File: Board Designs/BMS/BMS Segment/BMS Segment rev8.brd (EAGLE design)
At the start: 108 x 247.1 mm, 267 parts

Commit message: Moved 6804 inward, fixed clearance issues
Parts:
- moved RU1_A 37.3 mm to (65.0, 228.6)
- moved J1_A 9.02 mm to (105.7, 198.5)
- moved J2_A 9.02 mm to (103.8, 198.5)
- moved J3_A 9.02 mm to (101.9, 198.5)
- moved J4_A 9.02 mm to (100.0, 198.5)
- moved J5_A 9.02 mm to (98.1, 198.5)
- moved J6_A 9.02 mm to (96.2, 198.5)
- moved J7_A 9.02 mm to (94.3, 198.5)
- moved J8_A 9.02 mm to (92.4, 198.5)
- moved C1_A 7.62 mm to (104.8, 179.3)
- moved RB1_A 7.62 mm to (104.8, 188.8)
- moved RB2_A 7.62 mm to (104.8, 185.7)
- moved U$1 7.62 mm to (94.7, 185.1)
- moved C2_A 7.62 mm to (104.8, 182.5)
- moved C6_A 7.62 mm to (94.3, 194.1)
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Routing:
- net V-_A: track 804.3 -> 746.8 mm
- net UNUSED1_A: track 95.2 -> 64.8 mm
- net S5_B: track 136.6 -> 106.6 mm
- net V-_B: track 708.3 -> 685.2 mm
- net GPIO4_A: track 65.9 -> 76.6 mm
- net VREG_A: track 76.9 -> 66.9 mm
- net SENSE18: track 140.5 -> 132.8 mm
- net GPIO1_A: track 192.4 -> 200.1 mm
- net GPIO3_A: track 126.2 -> 133.9 mm
- net GPIO2_A: track 180.2 -> 187.9 mm
- net C9_A: track 67.8 -> 75.5 mm
- net C10_A: track 64.9 -> 72.5 mm
- net S9_A: track 71.1 -> 78.7 mm
- net C3_A: track 39.3 -> 31.8 mm
- net S3_A: track 32.9 -> 25.3 mm
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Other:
- board text added: "x1"
- board text added: "x2"
- board text added: "x4"
- board text added: "x8"

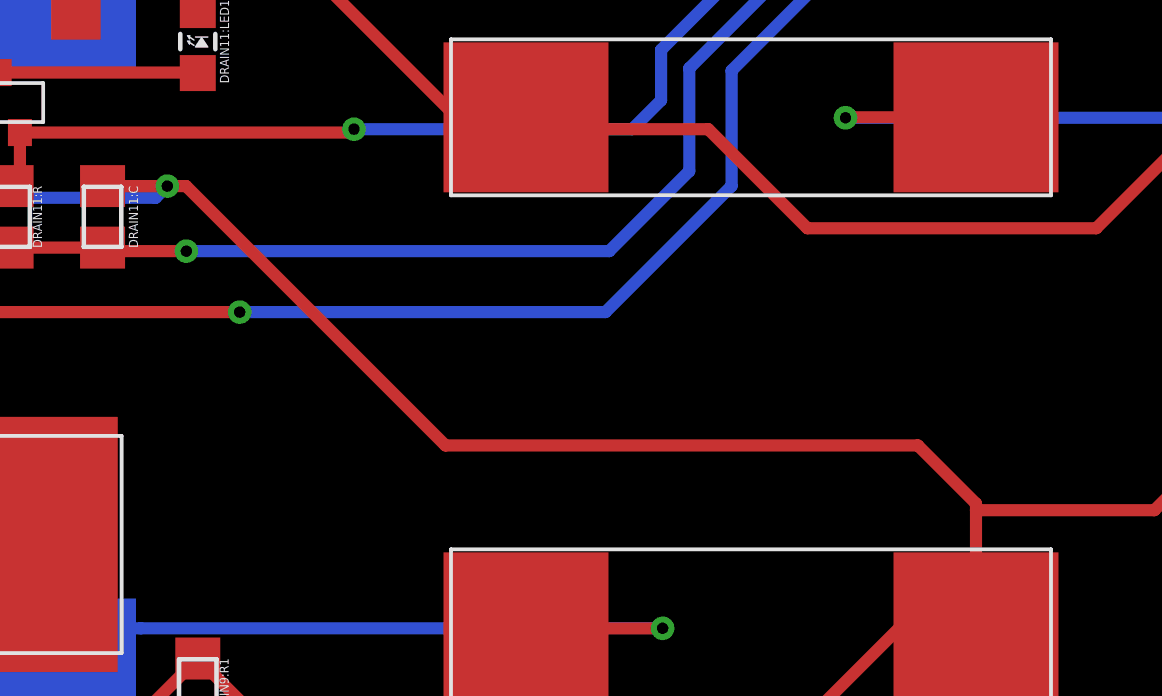
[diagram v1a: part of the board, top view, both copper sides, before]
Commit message: Changed resistor values to K, M, R convention. Changed texts to vector font
Eagle has the greek symbol ohm on the schematic and board in proportional font, but it does not have it in vector font. CAM processor seems to automatically convert to vector front and all the ohm symbol shows up as ? on the silkscreen.
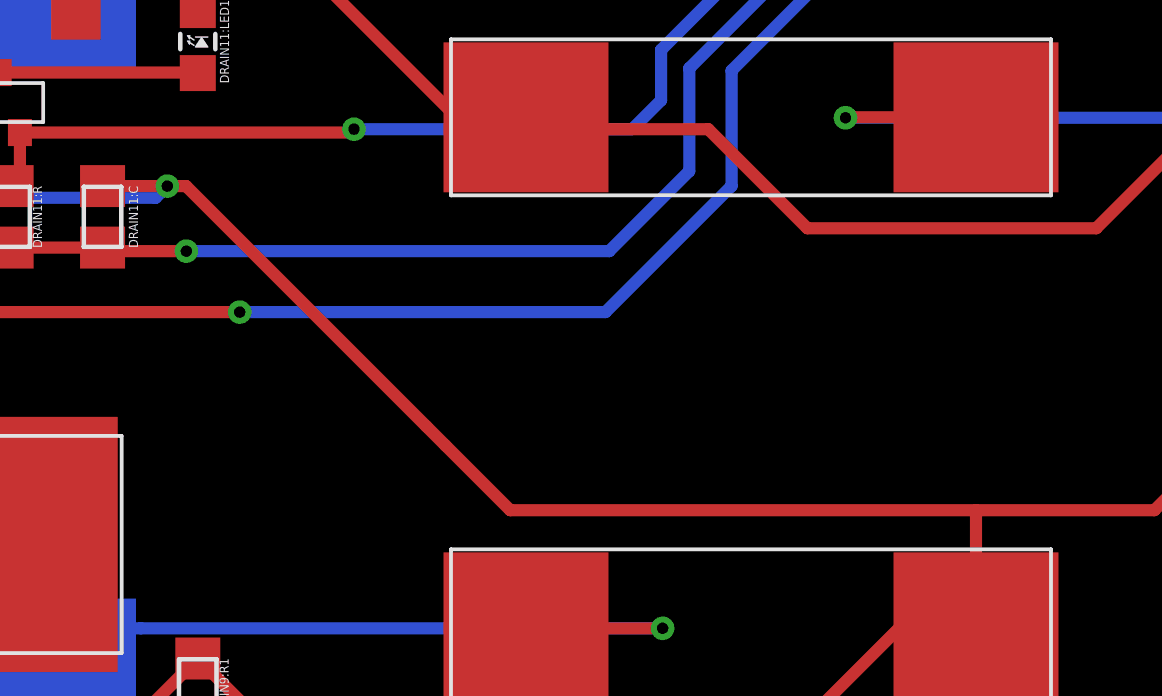
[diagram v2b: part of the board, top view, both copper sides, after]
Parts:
- DRAIN10:DISCHARGE, DRAIN11:DISCHARGE, DRAIN12:DISCHARGE, DRAIN13:DISCHARGE, DRAIN14:DISCHARGE, DRAIN15:DISCHARGE, DRAIN16:DISCHARGE, DRAIN17:DISCHARGE, DRAIN18:DISCHARGE, DRAIN1:DISCHARGE, DRAIN2:DISCHARGE, DRAIN3:DISCHARGE, DRAIN4:DISCHARGE, DRAIN5:DISCHARGE, DRAIN6:DISCHARGE, DRAIN7:DISCHARGE, DRAIN8:DISCHARGE, DRAIN9:DISCHARGE: value 5Ω -> 5R
- DRAIN10:GATE, DRAIN11:GATE, DRAIN12:GATE, DRAIN13:GATE, DRAIN14:GATE, DRAIN15:GATE, DRAIN16:GATE, DRAIN17:GATE, DRAIN18:GATE, DRAIN1:GATE, DRAIN2:GATE, DRAIN3:GATE, DRAIN4:GATE, DRAIN5:GATE, DRAIN6:GATE, DRAIN7:GATE, DRAIN8:GATE, DRAIN9:GATE: value 3.3kΩ -> 3K3
- DRAIN10:R, DRAIN11:R, DRAIN12:R, DRAIN13:R, DRAIN14:R, DRAIN15:R, DRAIN16:R, DRAIN17:R, DRAIN18:R, DRAIN1:R, DRAIN2:R, DRAIN3:R, DRAIN4:R, DRAIN5:R, DRAIN6:R, DRAIN7:R, DRAIN8:R, DRAIN9:R, R1_A, R1_B, R2_A, R2_B, RIN_A, RIN_B, RM_A, RM_B, RU1_A, RU1_B, THERM_FILTER10:R, THERM_FILTER1:R, THERM_FILTER2:R, THERM_FILTER3:R, THERM_FILTER4:R, THERM_FILTER5:R, THERM_FILTER6:R, THERM_FILTER7:R, THERM_FILTER8:R, THERM_FILTER9:R: value 100Ω -> 100R
- DRAIN10:R1, DRAIN11:R1, DRAIN12:R1, DRAIN13:R1, DRAIN14:R1, DRAIN15:R1, DRAIN16:R1, DRAIN17:R1, DRAIN18:R1, DRAIN1:R1, DRAIN2:R1, DRAIN3:R1, DRAIN4:R1, DRAIN5:R1, DRAIN6:R1, DRAIN7:R1, DRAIN8:R1, DRAIN9:R1: value 150Ω -> 150R
- R3_A, R3_B: value 402Ω -> 402R
- R4_A, R4_B, R5_A, R5_B: value 22Ω -> 22R
- RB1_A, RB1_B: value 1.2kΩ -> 1K2
- RB2_A, RB2_B: value 800Ω -> 800R
- THERM1, THERM2, THERM3, THERM4, THERM_FILTER10:R1, THERM_FILTER1:R1, THERM_FILTER2:R1, THERM_FILTER3:R1, THERM_FILTER4:R1, THERM_FILTER5:R1, THERM_FILTER6:R1, THERM_FILTER7:R1, THERM_FILTER8:R1, THERM_FILTER9:R1: value 10kΩ -> 10K

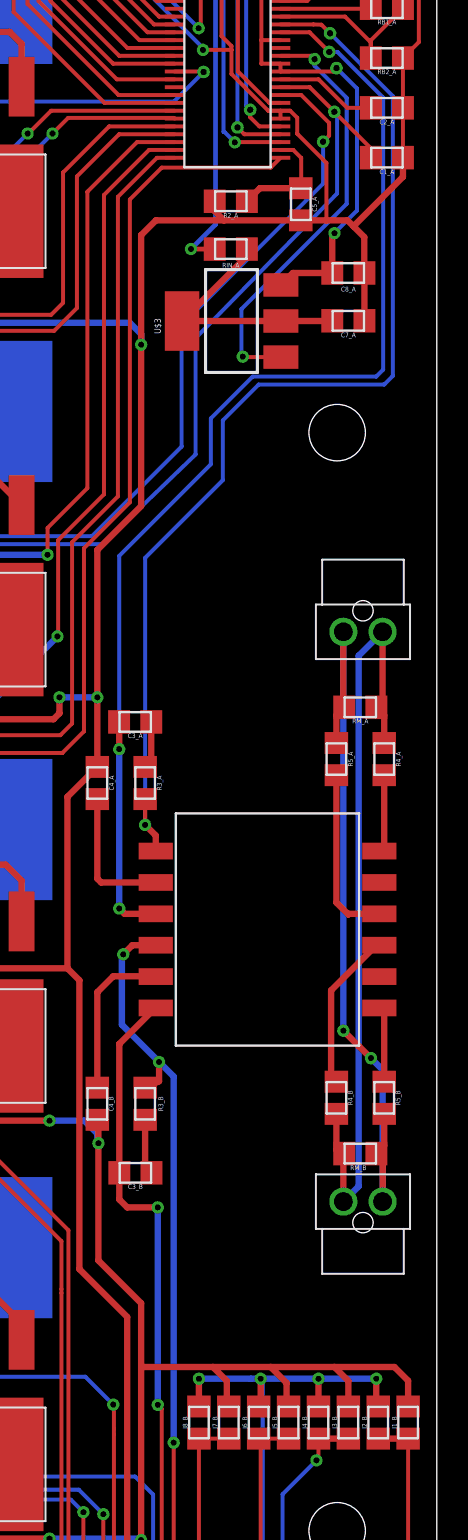
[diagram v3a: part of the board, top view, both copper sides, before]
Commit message: Silkscreen modifications, small adjustments to trace locations
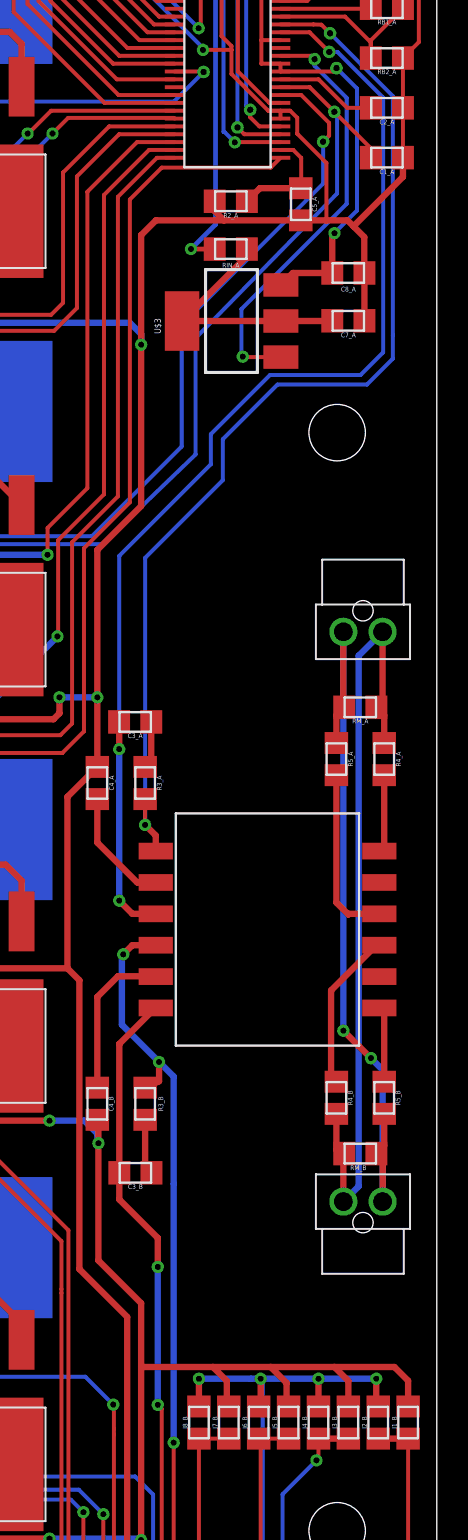
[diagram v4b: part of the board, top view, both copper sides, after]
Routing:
- net IM_A: track 75.9 -> 74.2 mm
- net IP_A: track 70.3 -> 69.0 mm
- net N$21: track 8.90 -> 7.55 mm
- net IM_B: track 59.0 -> 57.8 mm
